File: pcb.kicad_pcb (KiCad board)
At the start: 2 copper layers, 76 parts, among them SW1 SW_Push, U1 ATmega32U4-AU, Y1 16MHz

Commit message: Made A Mess
Made A Mess
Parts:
- moved SW1 131.5 mm to (156.2, 121.9), turned to 180 degrees
- moved C2 125.4 mm to (148.5, 131.7)
- moved C3 125.4 mm to (148.6, 126.9)
- moved C7 125.4 mm to (148.6, 121.9)
- moved C1 125.4 mm to (148.6, 136.6)
- moved R4 23.3 mm to (141.0, 121.9), turned to 0 degrees
- moved C4 20.6 mm to (157.5, 114.3), turned to 90 degrees
- moved C5 20.3 mm to (157.5, 110.5), turned to -90 degrees
- moved Y1 19.3 mm to (161.3, 111.8)
- moved R3 17.1 mm to (154.9, 105.4), turned to 90 degrees
- moved R2 14.2 mm to (139.7, 99.1)
- moved F1 11.6 mm to (137.2, 99.1), turned to 90 degrees
- moved R1 10.1 mm to (142.2, 99.1)
- moved C6 6.98 mm to (144.8, 99.1), turned to 180 degrees
- moved U1 5.94 mm to (146.1, 110.5), turned to -90 degrees
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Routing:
- net GND: track 0.00 -> 68.4 mm
- net +5V: track 0.00 -> 31.8 mm
- net Net-(R3-Pad2): track 0.00 -> 30.8 mm
- net Net-(C5-Pad1): track 0.00 -> 11.7 mm
- net Net-(C4-Pad1): track 0.00 -> 11.6 mm
- net Net-(R2-Pad1): track 0.00 -> 7.31 mm
- net Net-(C6-Pad1): track 0.00 -> 5.87 mm
- net Net-(R4-Pad2): track 0.00 -> 5.79 mm
- net Net-(R1-Pad1): track 0.00 -> 5.71 mm
- net D+: track 0.00 -> 5.25 mm
- net VCC: track 0.00 -> 5.18 mm
- net D-: track 0.00 -> 4.92 mm

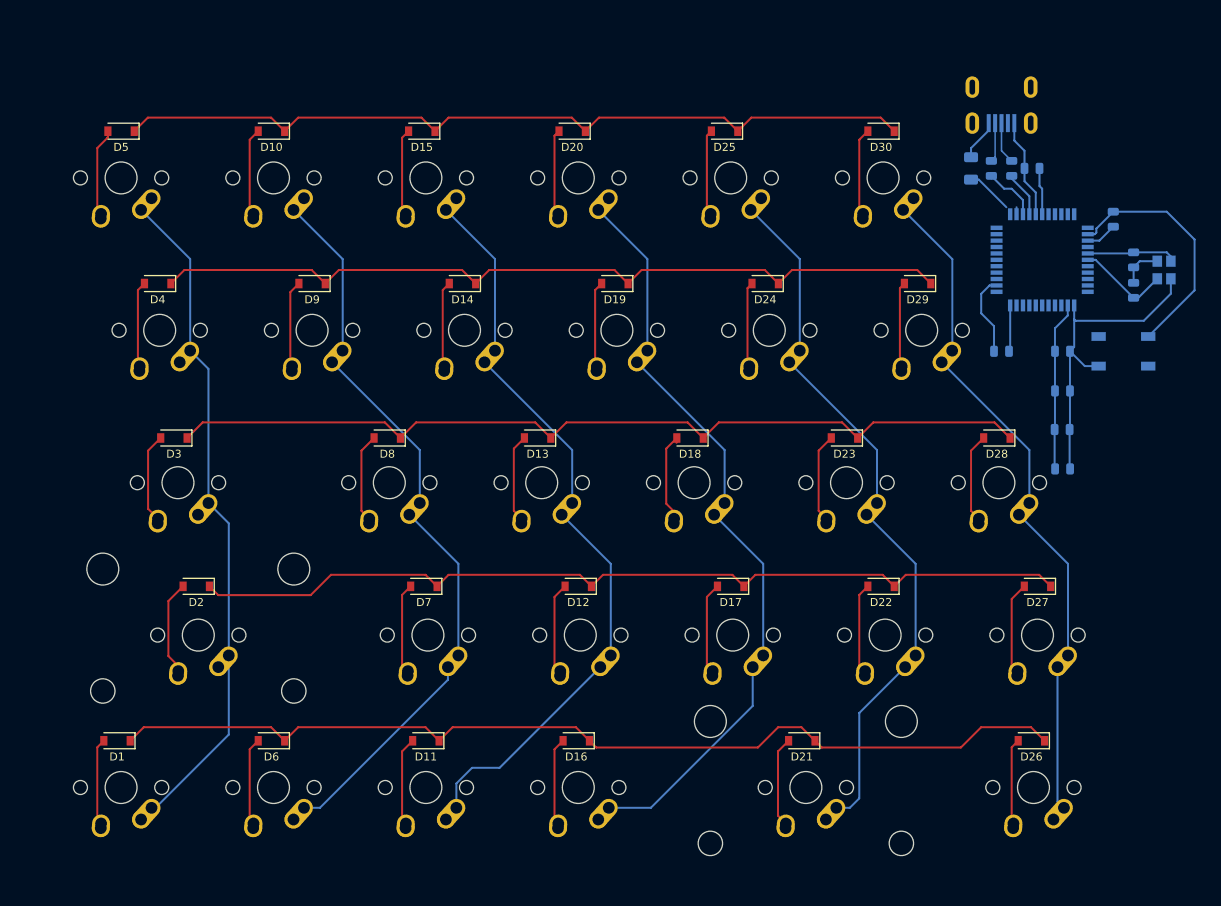
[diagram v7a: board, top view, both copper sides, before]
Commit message: Added GND Zone
Added GND Zone
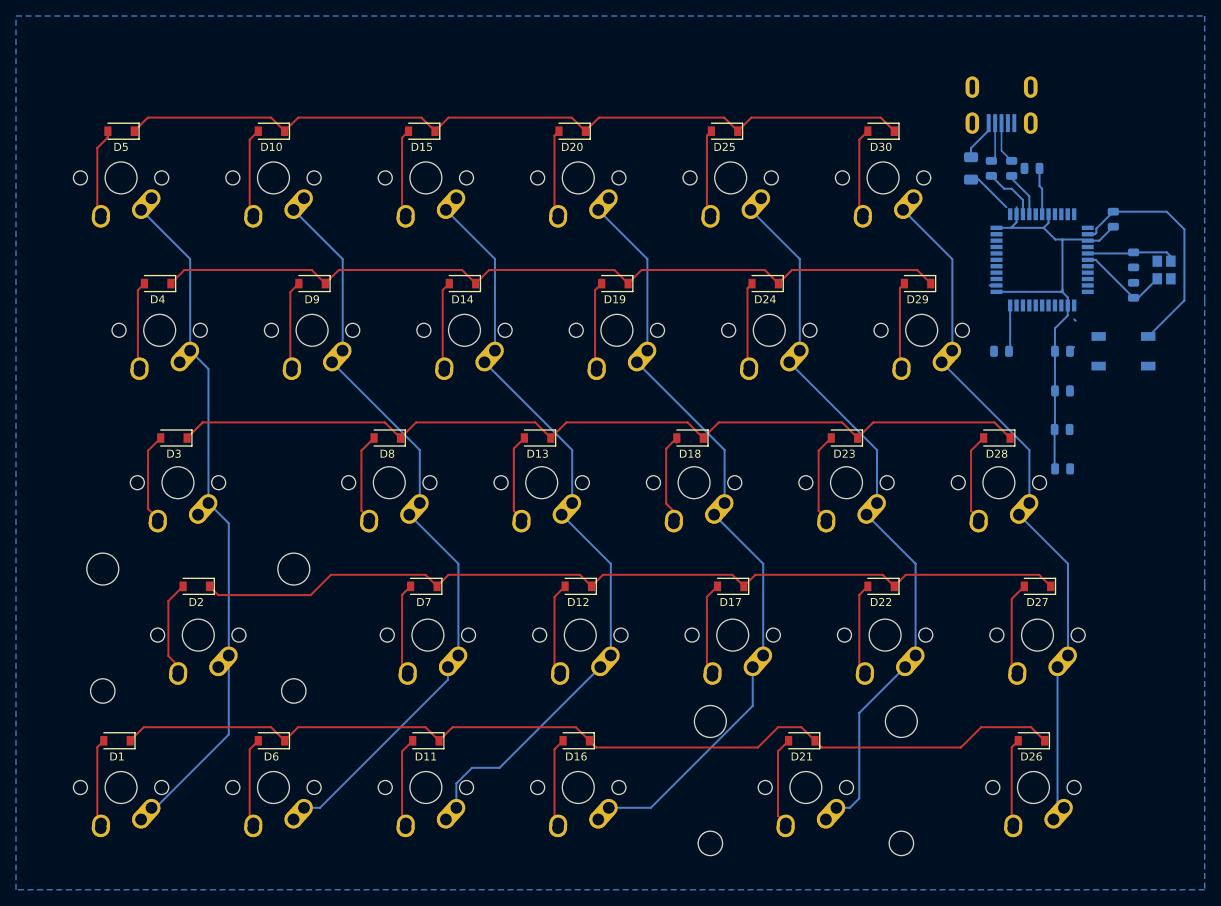
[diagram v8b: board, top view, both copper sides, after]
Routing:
- net GND: track 68.4 -> 2.04 mm
- net +5V: track 31.8 -> 63.9 mm
- net Net-(R3-Pad2): track 30.8 -> 29.7 mm
- added copper zone on B.Cu, net GND
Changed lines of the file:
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@@
     )
   )
-  (segment (start 157.48 111.4275) (end 157.48 113.3625) (width 0.25) (layer "B.Cu") (net 1))
-  (segment (start 143.8425 96.8525) (end 143.8425 99.06) (width 0.25) (layer "B.Cu") (net 1))
-  (segment (start 138.43 117.1725) (end 138.43 114.735) (width 0.25) (layer "B.Cu") (net 1))
-  (segment (start 142.57 95.58) (end 143.8425 96.8525) (width 0.25) (layer "B.Cu") (net 1))
-  (segment (start 149.5275 121.92) (end 149.5275 126.873) (width 0.25) (layer "B.Cu") (net 1))
-  (segment (start 143.8425 100.6625) (end 145.25 102.07) (width 0.25) (layer "B.Cu") (net 1))
-  (segment (start 151.3775 123.77) (end 149.5275 121.92) (width 0.25) (layer "B.Cu") (net 1))
   (segment (start 149.5275 121.92) (end 150.05 121.3975) (width 0.25) (layer "B.Cu") (net 1))
-  (segment (start 149.479 131.699) (end 149.479 136.55675) (width 0.25) (layer "B.Cu") (net 1))
-  (segment (start 142.57 93.4) (end 142.57 95.58) (width 0.25) (layer "B.Cu") (net 1))
   (segment (start 149.5275 131.6505) (end 149.479 131.699) (width 0.25) (layer "B.Cu") (net 1))
   (segment (start 149.479 136.55675) (end 149.5425 136.62025) (width 0.25) (layer "B.Cu") (net 1))
-  (segment (start 138.43 114.735) (end 139.475 113.69) (width 0.25) (layer "B.Cu") (net 1))
   (segment (start 150.24 118.11) (end 150.05 117.92) (width 0.25) (layer "B.Cu") (net 1))
-  (segment (start 145.25 102.07) (end 145.25 104.79) (width 0.25) (layer "B.Cu") (net 1))
-  (segment (start 158.75 118.11) (end 150.24 118.11) (width 0.25) (layer "B.Cu") (net 1))
-  (segment (start 143.8425 99.06) (end 143.8425 100.6625) (width 0.25) (layer "B.Cu") (net 1))
-  (segment (start 153.11 123.77) (end 151.3775 123.77) (width 0.25) (layer "B.Cu") (net 1))
-  (segment (start 162.14 112.86) (end 162.14 114.72) (width 0.25) (layer "B.Cu") (net 1))
-  (segment (start 160.44 110.66) (end 158.2475 110.66) (width 0.25) (layer "B.Cu") (net 1))
-  (segment (start 140.0325 118.775) (end 138.43 117.1725) (width 0.25) (layer "B.Cu") (net 1))
   (segment (start 139.475 113.69) (end 140.35 113.69) (width 0.25) (layer "B.Cu") (net 1))
-  (segment (start 150.05 121.3975) (end 150.05 117.92) (width 0.25) (layer "B.Cu") (net 1))
-  (segment (start 158.2475 110.66) (end 157.48 111.4275) (width 0.25) (layer "B.Cu") (net 1))
-  (segment (start 149.5275 126.873) (end 149.5275 131.6505) (width 0.25) (layer "B.Cu") (net 1))
-  (segment (start 150.05 117.92) (end 150.05 116.19) (width 0.25) (layer "B.Cu") (net 1))
-  (segment (start 162.14 114.72) (end 158.75 118.11) (width 0.25) (layer "B.Cu") (net 1))
-  (segment (start 140.0325 121.92) (end 140.0325 118.775) (width 0.25) (layer "B.Cu") (net 1))
+  (segment (start 146.85 105.88) (end 146.85 104.79) (width 0.25) (layer "B.Cu") (net 2))
   (segment (start 147.6525 126.873) (end 147.6525 131.6505) (width 0.25) (layer "B.Cu") (net 2))
+  (segment (start 147.7 107.95) (end 148.59 107.95) (width 0.25) (layer "B.Cu") (net 2))
+  (segment (start 149.25 115.19) (end 148.59 114.53) (width 0.25) (layer "B.Cu") (net 2))
+  (segment (start 146.24 106.49) (end 147.7 107.95) (width 0.25) (layer "B.Cu") (net 2))
+  (segment (start 140.35 114.49) (end 148.4 114.49) (width 0.25) (layer "B.Cu") (net 2))
   (segment (start 147.604 131.699) (end 147.604 136.55675) (width 0.25) (layer "B.Cu") (net 2))
   (segment (start 137.16 100.46) (end 138.125 100.46) (width 0.25) (layer "B.Cu") (net 2))
+  (segment (start 148.59 107.95) (end 151.13 107.95) (width 0.25) (layer "B.Cu") (net 2))
   (segment (start 147.6525 121.92) (end 147.6525 126.873) (width 0.25) (layer "B.Cu") (net 2))
+  (segment (start 148.59 114.3) (end 148.59 107.95) (width 0.25) (layer "B.Cu") (net 2))
+  (segment (start 142.85 105.79) (end 142.15 106.49) (width 0.25) (layer "B.Cu") (net 2))
+  (segment (start 142.15 106.49) (end 140.35 106.49) (width 0.25) (layer "B.Cu") (net 2))
   (segment (start 147.6525 121.92) (end 147.6525 119.0475) (width 0.25) (layer "B.Cu") (net 2))
   (segment (start 138.125 100.46) (end 141.58 103.915) (width 0.25) (layer "B.Cu") (net 2))
   (segment (start 147.6525 119.0475) (end 149.25 117.45) (width 0.25) (layer "B.Cu") (net 2))
+  (segment (start 148.59 114.53) (end 148.59 114.3) (width 0.25) (layer "B.Cu") (net 2))
   (segment (start 147.604 136.55675) (end 147.6675 136.62025) (width 0.25) (layer "B.Cu") (net 2))
+  (segment (start 149.25 116.19) (end 149.25 115.19) (width 0.25) (layer "B.Cu") (net 2))
+  (segment (start 142.85 104.79) (end 142.85 105.79) (width 0.25) (layer "B.Cu") (net 2))
   (segment (start 154.94 106.3475) (end 153.1975 108.09) (width 0.25) (layer "B.Cu") (net 2))
   (segment (start 147.6525 131.6505) (end 147.604 131.699) (width 0.25) (layer "B.Cu") (net 2))
   (segment (start 142.85 103.915) (end 142.85 104.79) (width 0.25) (layer "B.Cu") (net 2))
+  (segment (start 146.24 106.49) (end 146.85 105.88) (width 0.25) (layer "B.Cu") (net 2))
+  (segment (start 142.15 106.49) (end 146.24 106.49) (width 0.25) (layer "B.Cu") (net 2))
+  (segment (start 148.4 114.49) (end 148.59 114.3) (width 0.25) (layer "B.Cu") (net 2))
   (segment (start 153.1975 108.09) (end 151.75 108.09) (width 0.25) (layer "B.Cu") (net 2))
   (segment (start 149.25 117.45) (end 149.25 116.19) (width 0.25) (layer "B.Cu") (net 2))
@@
   (segment (start 142.24 101.6) (end 143.65 103.01) (width 0.25) (layer "B.Cu") (net 51))
   (segment (start 152.825 107.09) (end 152.625 107.29) (width 0.25) (layer "B.Cu") (net 52))
-  (segment (start 159.33 120.07) (end 165.1 114.3) (width 0.25) (layer "B.Cu") (net 52))
+  (segment (start 163.83 106.68) (end 161.6225 104.4725) (width 0.25) (layer "B.Cu") (net 52))
+  (segment (start 159.33 120.07) (end 163.83 115.57) (width 0.25) (layer "B.Cu") (net 52))
   (segment (start 154.94 104.4725) (end 152.825 106.5875) (width 0.25) (layer "B.Cu") (net 52))
-  (segment (start 165.1 107.95) (end 161.6225 104.4725) (width 0.25) (layer "B.Cu") (net 52))
-  (segment (start 161.6225 104.4725) (end 154.94 104.4725) (width 0.25) (layer "B.Cu") (net 52))
   (segment (start 152.825 106.5875) (end 152.825 107.09) (width 0.25) (layer "B.Cu") (net 52))
   (segment (start 152.625 107.29) (end 151.75 107.29) (width 0.25) (layer "B.Cu") (net 52))
-  (segment (start 165.1 114.3) (end 165.1 107.95) (width 0.25) (layer "B.Cu") (net 52))
+  (segment (start 161.6225 104.4725) (end 154.94 104.4725) (width 0.25) (layer "B.Cu") (net 52))
   (segment (start 159.31 120.07) (end 159.33 120.07) (width 0.25) (layer "B.Cu") (net 52))
+  (segment (start 163.83 115.57) (end 163.83 106.68) (width 0.25) (layer "B.Cu") (net 52))
   (segment (start 142.05 121.7775) (end 142.05 116.19) (width 0.25) (layer "B.Cu") (net 53))
   (segment (start 141.9075 121.92) (end 142.05 121.7775) (width 0.25) (layer "B.Cu") (net 53))
+  (zone (net 1) (net_name "GND") (layer "B.Cu") (name "GND") (hatch edge 0.508)
+    (connect_pads (clearance 0.127))
+    (min_thickness 0.254) (filled_areas_thickness no)
+    (fill yes (thermal_gap 0.508) (thermal_bridge_width 0.508))
+    (polygon
+      (pts
+        (xy 166.37 115.57)
+        (xy 166.37 151.13)
+        (xy 166.37 189.23)
+        (xy 17.78 189.23)
+        (xy 17.78 80.01)
+        (xy 166.37 80.01)
+      )
+    )
+  )
   (group "" (id 386d9108-238b-4180-9c73-1d27ca21ca0c)
     (members
